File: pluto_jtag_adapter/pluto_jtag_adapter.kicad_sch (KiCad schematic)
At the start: 50 parts, among them J1 JTAG_UART_PLUTO, J2 Conn_01x08, J3 Conn_01x04, J4 USB_B_Micro, U1 FT2232HL, U2 AP2112K-3.3, U3 AP2112K-1.8, U4 93LC46B, U5 TXB0102DCT, U6 TXB0104D, Y1 7M-12.000MAAJ-T

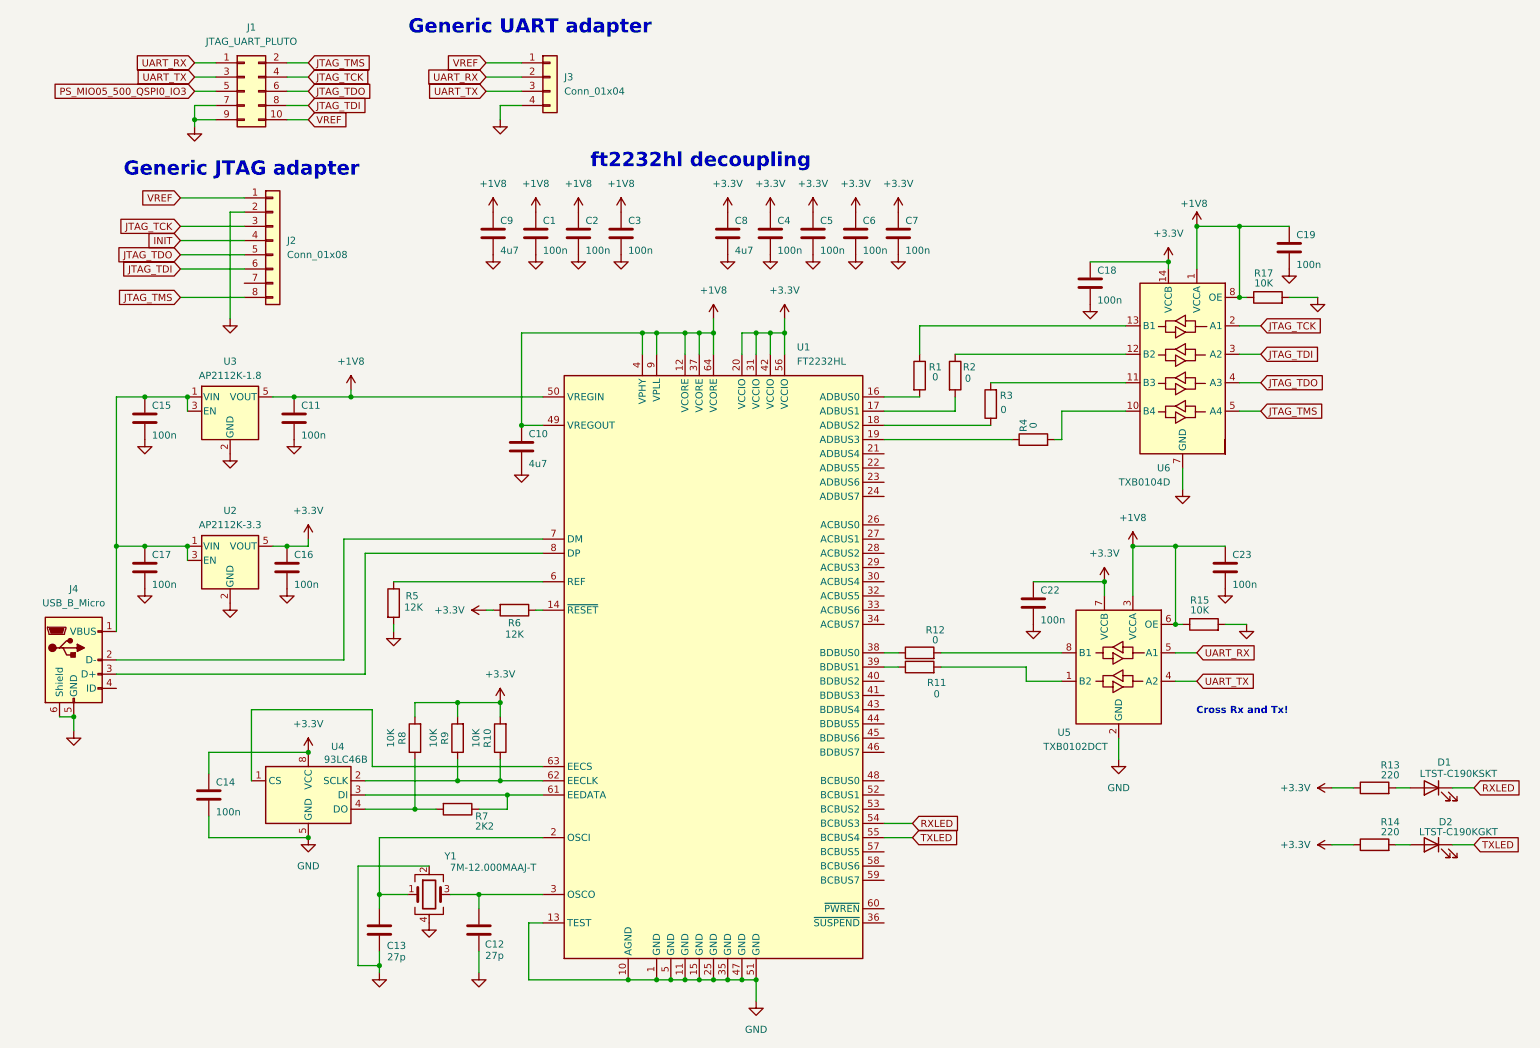
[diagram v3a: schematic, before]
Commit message: Clean up PCB layout, add mounting holes and header pin names
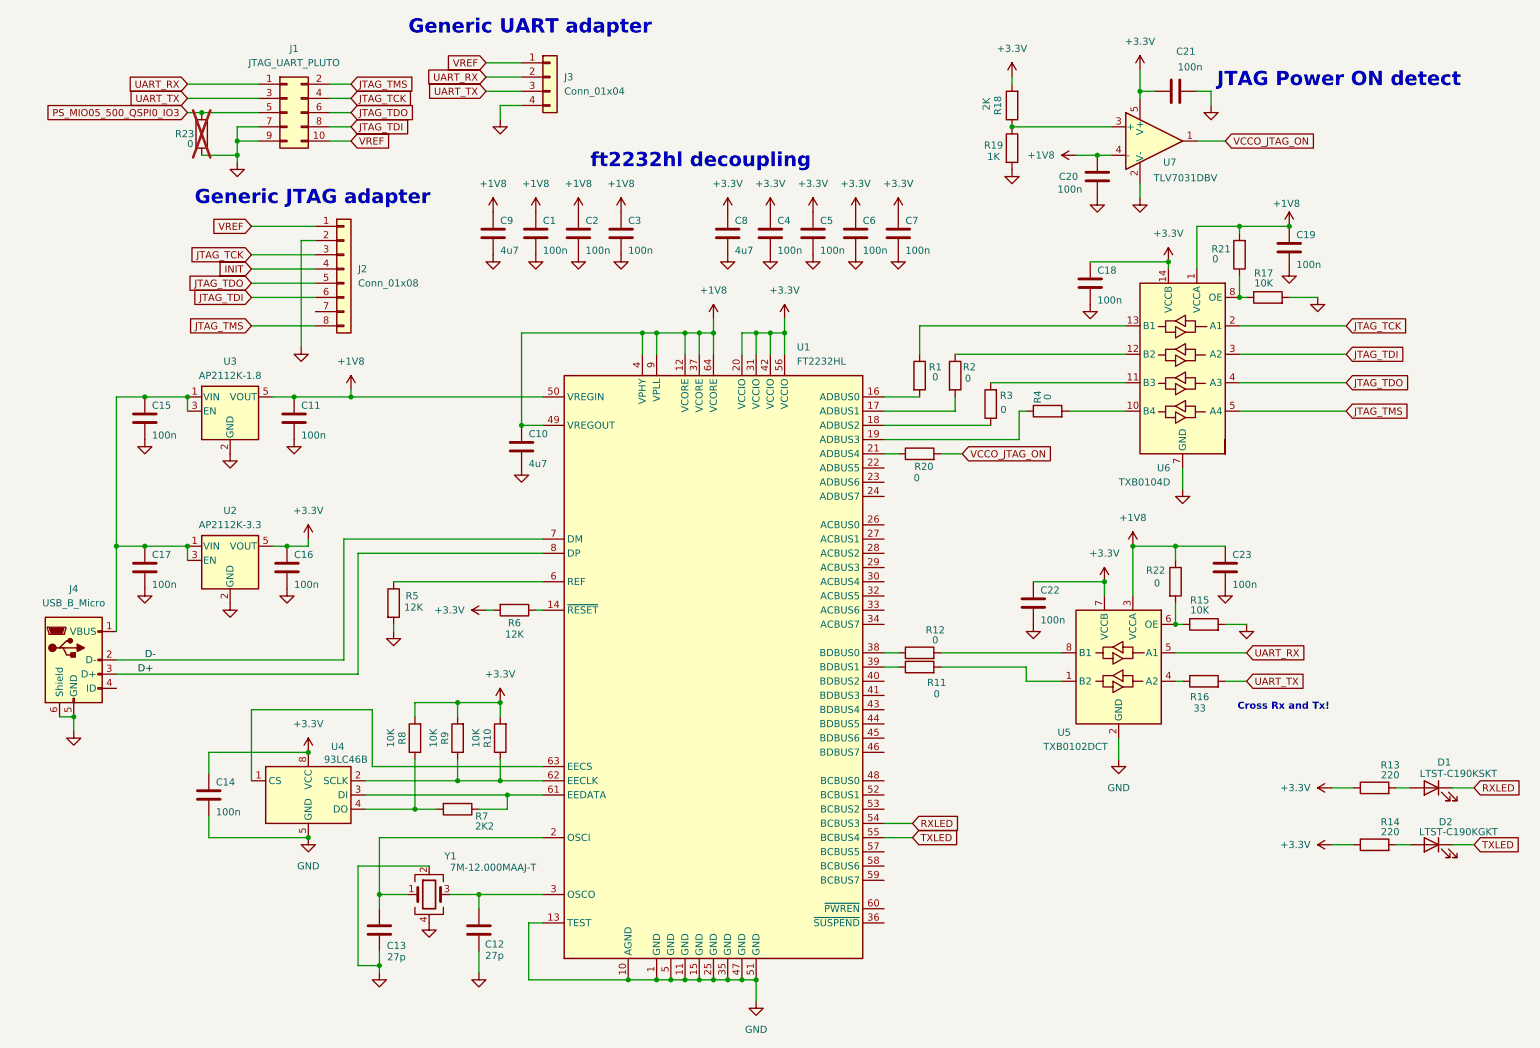
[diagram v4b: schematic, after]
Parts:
- added C20, C21: 100n, Capacitor_SMD:C_0603_1608Metric_Pad1.08x0.95mm_HandSolder, symbol Device:C
- added R16: 33, Resistor_SMD:R_0603_1608Metric_Pad0.98x0.95mm_HandSolder, symbol Device:R
- added R18: 2K, Resistor_SMD:R_0603_1608Metric_Pad0.98x0.95mm_HandSolder, symbol Device:R
- added R19: 1K, Resistor_SMD:R_0603_1608Metric_Pad0.98x0.95mm_HandSolder, symbol Device:R
- added R20, R21, R22, R23: 0, Resistor_SMD:R_0603_1608Metric_Pad0.98x0.95mm_HandSolder, symbol Device:R
- added U7: TLV7031DBV, Package_TO_SOT_SMD:SOT-23-5, symbol Comparator:TLV7031DBV
- J4: footprint Connector_USB:USB_Micro-B_Amphenol_10118194_Horizontal -> Connector_USB:USB_Micro-B_Molex_47346-0001
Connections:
- net +1V8: now also C20.1, R21.2, R22.1, U7.4 (-); no longer R15.1, R17.1, U5.6 (OE), U6.8 (OE)
- net +3.3V: now also C21.1, R18.2, U7.5 (V+)
- net GND: now also C20.2, C21.2, R19.2, R23.1, U7.2 (V-)
- net PS_MIO05_500_QSPI0_IO3: now also R23.2
- net UART_TX: now also R16.2; no longer U5.4 (A2)
- net D-: now reaches J4.2 (D-), U1.7 (DM)
- net D+: now reaches J4.3 (D+), U1.8 (DP)
- net at U1.21 (ADBUS4): now also R20.1
- new net: R16.1, U5.4 (A2)
- new net: R15.1, R22.2, U5.6 (OE)
- new net: R17.1, R21.1, U6.8 (OE)
- new net: R18.1, R19.1, U7.3 (+)
- new net VCCO_JTAG_ON: R20.2, U7.1
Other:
- note added: "JTAG Power ON detect"
- company: (none) -> Teodor Dimitrov
- title: (none) -> Pluto JTAG Adapter
- moved on the sheet: J1, J2, R4

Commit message: Add ground fill on top layer. Improve ground fill around signals
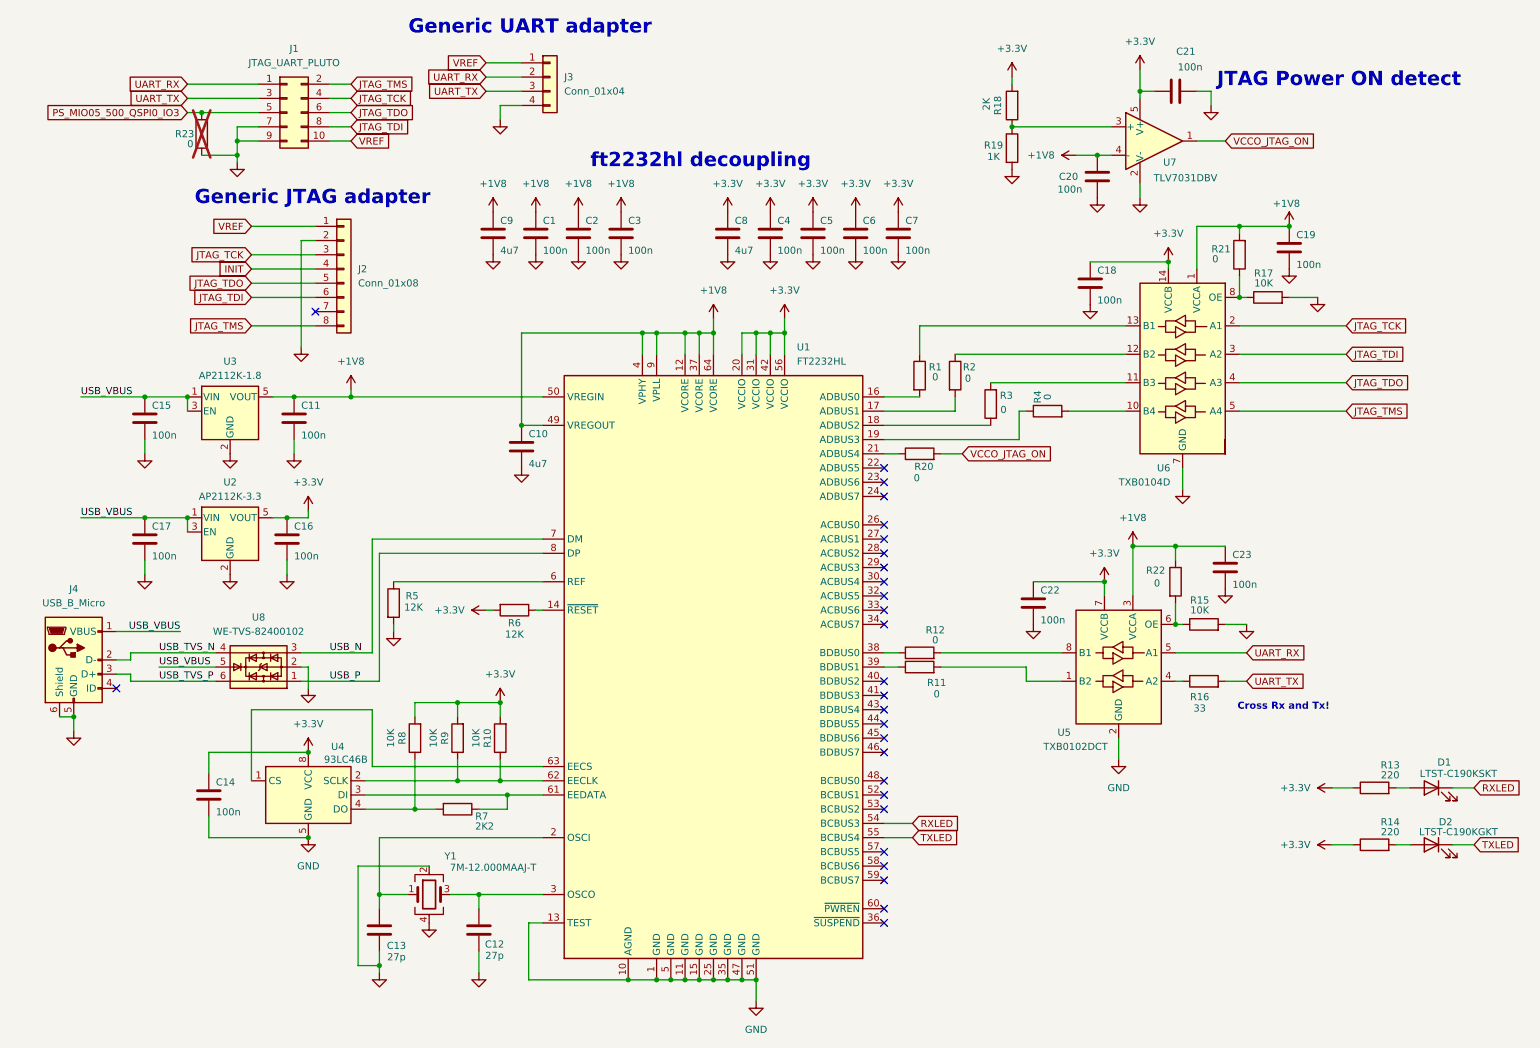
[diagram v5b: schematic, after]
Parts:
- added U8: WE-TVS-82400102, Package_TO_SOT_SMD:SOT-23-6, symbol Power_Protection:WE-TVS-82400102
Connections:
- net GND: now also U8.2
- net USB_VBUS: now reaches C15.1, C17.1, J4.1 (VBUS), U2.1 (VIN), U2.3 (EN), U3.1 (VIN), U3.3 (EN)
- net USB_VBUS: now also U8.5
- net D+ renamed USB_P
- net USB_P: now also U8.1; no longer J4.3 (D+)
- net D- renamed USB_N
- net USB_N: now also U8.3; no longer J4.2 (D-)
- new net USB_TVS_N: J4.2 (D-), U8.4
- new net USB_TVS_P: J4.3 (D+), U8.6
- no-connect marks 0 -> 27
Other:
- moved on the sheet: C16, C17, U2

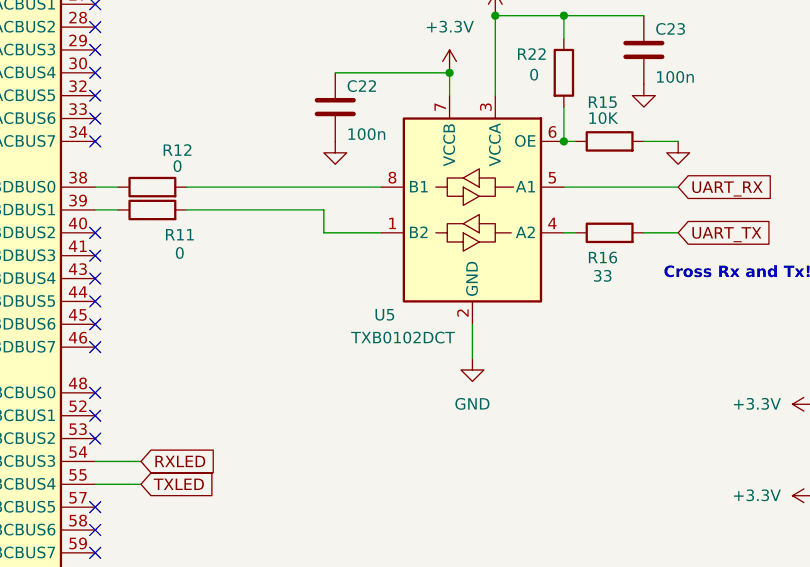
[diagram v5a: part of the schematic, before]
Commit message: Replace obsolete component TXB0102DCT with TXB0102DCU
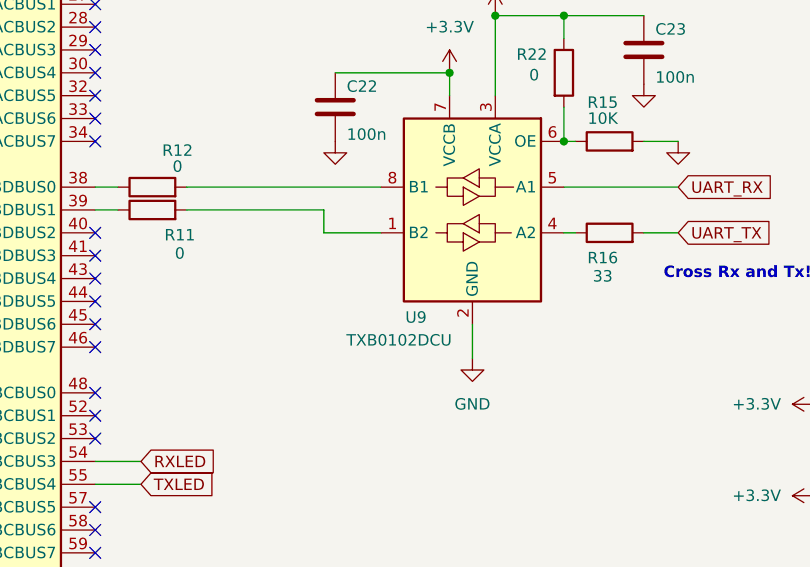
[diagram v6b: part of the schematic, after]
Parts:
- removed U5: TXB0102DCT, Package_SO:TSSOP-8_3x3mm_P0.65mm, symbol Logic_LevelTranslator:TXB0102DCT
- added U9: TXB0102DCU, Package_SO:VSSOP-8_2.3x2mm_P0.5mm, symbol Logic_LevelTranslator:TXB0102DCU
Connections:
- net +1V8: now also U9.3 (VCCA)
- net +3.3V: now also U9.7 (VCCB)
- net GND: now also U9.2 (GND)
- net UART_RX: now also U9.5 (A1)
- net at R11.2: now also U9.1 (B2)
- net at R16.1: now also U9.4 (A2)
- net at R15.1, R22.2: now also U9.6 (OE)
- net at R12.2: now also U9.8 (B1)
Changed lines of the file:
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@@
 	)
 	(junction
-		(at 218.44 121.92)
-		(diameter 0)
-		(color 0 0 0 0)
-	)
-	(junction
 		(at 135.89 185.42)
 		(diameter 0)
@@
 	)
 	(junction
+		(at 218.44 121.92)
+		(diameter 0)
+		(color 0 0 0 0)
+	)
+	(junction
 		(at 125.73 185.42)
 		(diameter 0)
@@
 	)
 	(symbol
-		(lib_id "Logic_LevelTranslator:TXB0102DCT")
-		(at 208.28 129.54 0)
-		(mirror y)
-		(unit 1)
-		(exclude_from_sim no)
-		(in_bom yes)
-		(on_board yes)
-		(dnp no)
-		(property "Reference" "U5"
-			(at 197.358 141.224 0)
-			(effects
-				(font
-					(size 1.27 1.27)
-				)
-				(justify right)
-			)
-		)
-		(property "Value" "TXB0102DCT"
-			(at 194.818 143.764 0)
-			(effects
-				(font
-					(size 1.27 1.27)
-				)
-				(justify right)
-			)
-		)
-		(property "Footprint" "Package_SO:TSSOP-8_3x3mm_P0.65mm"
-			(at 208.28 143.51 0)
-			(effects
-				(font
-					(size 1.27 1.27)
-				)
-				(hide yes)
-			)
-		)
-		(property "Datasheet" "http://www.ti.com/lit/ds/symlink/txb0102.pdf"
-			(at 208.28 130.302 0)
-			(effects
-				(font
-					(size 1.27 1.27)
-				)
-				(hide yes)
-			)
-		)
-		(property "Description" "2-Bit Bidirectional Voltage-Level Translator With Auto Direction Sensing and ±15-kV ESD Protection, TSSOP-8"
-			(at 208.28 129.54 0)
-			(effects
-				(font
-					(size 1.27 1.27)
-				)
-				(hide yes)
-			)
-		)
-		(pin "5"
-		)
-		(pin "1"
-		)
-		(pin "2"
-		)
-		(pin "7"
-		)
-		(pin "8"
-		)
-		(pin "3"
-		)
-		(pin "4"
-		)
-		(pin "6"
-		)
-		(instances
-			(project ""
-				(path "/3be8ddee-85ba-421c-a851-ede1499a4287"
-					(reference "U5")
-					(unit 1)
-				)
-			)
-		)
-	)
-	(symbol
 		(lib_id "power:GND")
 		(at 104.14 55.88 0)
@@
 					(unit 1)
 				)
+			)
+		)
+	)
+	(symbol
+		(lib_id "Logic_LevelTranslator:TXB0102DCU")
+		(at 208.28 129.54 0)
+		(mirror y)
+		(unit 1)
+		(exclude_from_sim no)
+		(in_bom yes)
+		(on_board yes)
+		(dnp no)
+		(property "Reference" "U9"
+			(at 203.2 141.478 0)
+			(effects
+				(font
+					(size 1.27 1.27)
+				)
+				(justify left)
+			)
+		)
+		(property "Value" "TXB0102DCU"
+			(at 205.994 144.018 0)
+			(effects
+				(font
+					(size 1.27 1.27)
+				)
+				(justify left)
+			)
+		)
+		(property "Footprint" "Package_SO:VSSOP-8_2.3x2mm_P0.5mm"
+			(at 208.28 143.51 0)
+			(effects
+				(font
+					(size 1.27 1.27)
+				)
+				(hide yes)
+			)
+		)
+		(property "Datasheet" "http://www.ti.com/lit/ds/symlink/txb0102.pdf"
+			(at 208.28 130.302 0)
+			(effects
+				(font
+					(size 1.27 1.27)
+				)
+				(hide yes)
+			)
+		)
+		(property "Description" "2-Bit Bidirectional Voltage-Level Translator With Auto Direction Sensing and ±15-kV ESD Protection, VSSOP-8"
+			(at 208.28 129.54 0)
+			(effects
+				(font
+					(size 1.27 1.27)
+				)
+				(hide yes)
+			)
+		)
+		(pin "3"
+		)
+		(pin "1"
+		)
+		(pin "8"
+		)
+		(pin "2"
+		)
+		(pin "6"
+		)
+		(pin "7"
+		)
+		(pin "4"
+		)
+		(pin "5"
+		)
+		(instances
+			(project ""
+				(path "/3be8ddee-85ba-421c-a851-ede1499a4287"
+					(reference "U9")
+					(unit 1)
+				)
